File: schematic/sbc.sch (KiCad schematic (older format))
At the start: 17 parts

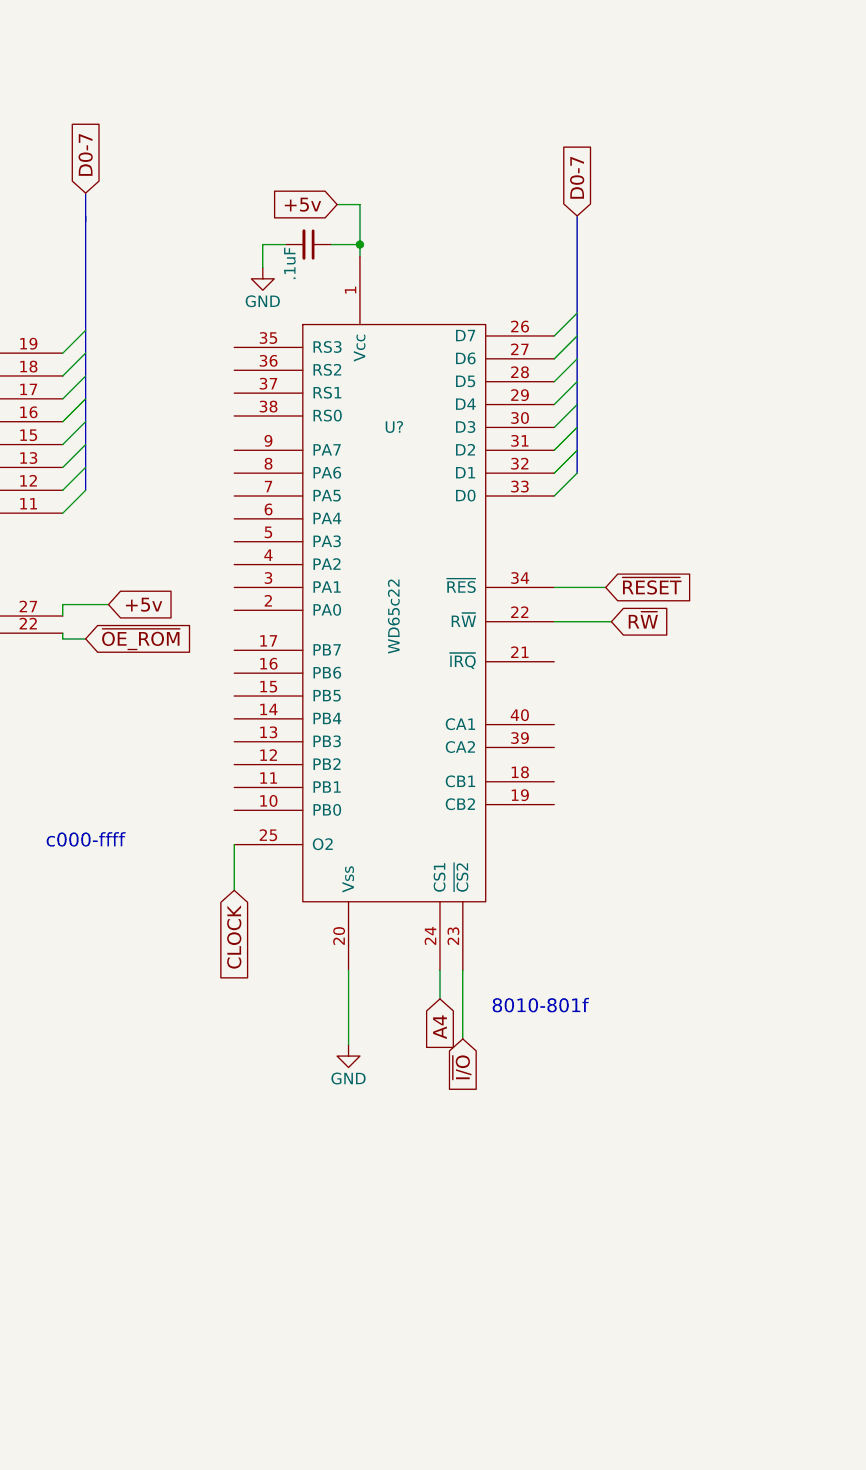
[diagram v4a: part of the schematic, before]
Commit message: Added LEDs to sbc schematic
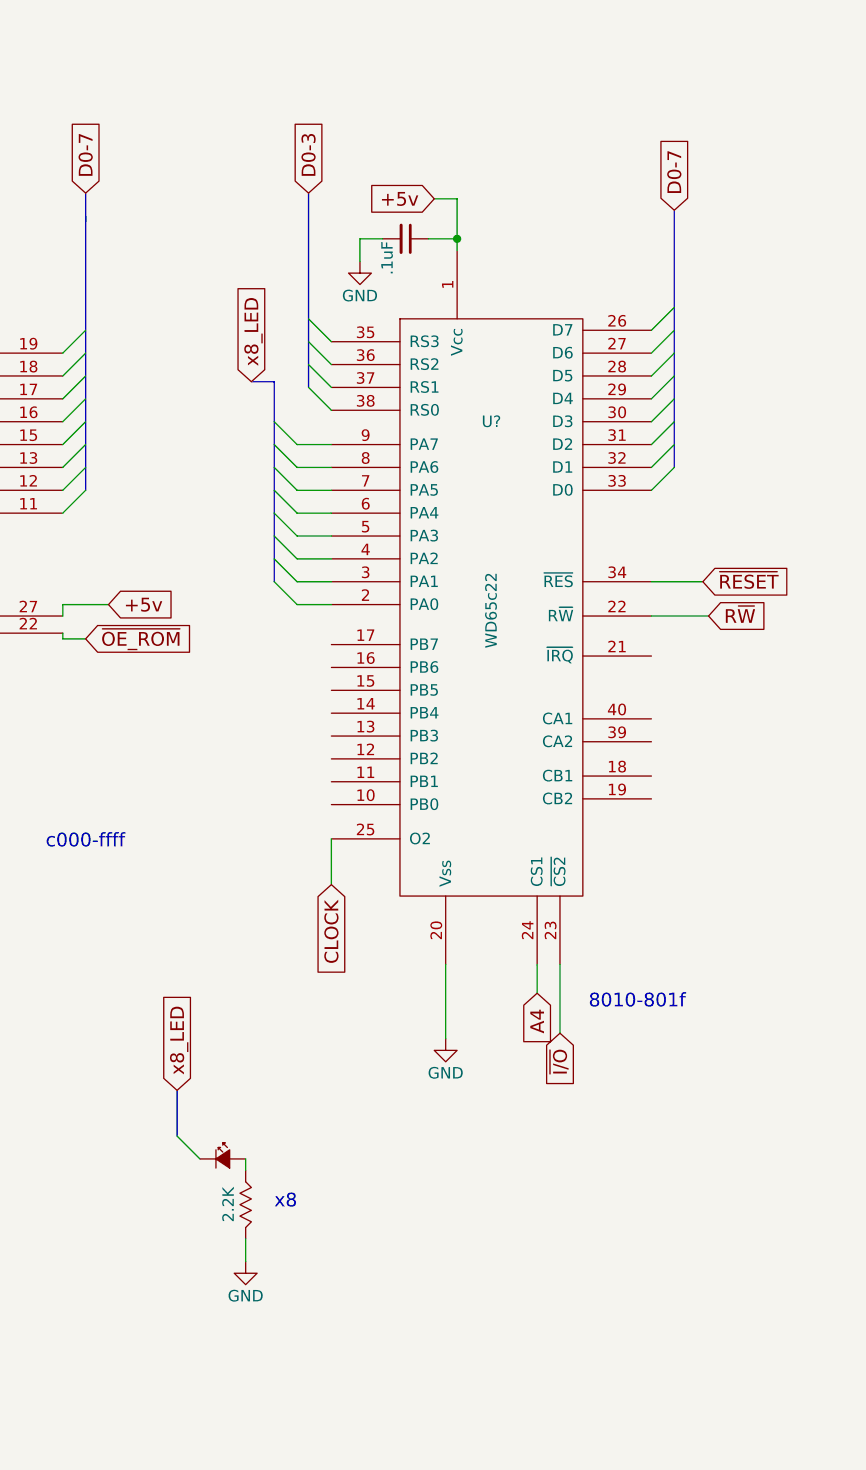
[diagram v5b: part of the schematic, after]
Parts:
- added D?: Led_Small, symbol Led_Small
- added R?: 2.2K, symbol Rsqig
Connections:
- net GND: now also R?.2
- new net: D?.2 (A), R?.1
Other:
- note added: "x8"
- moved on the sheet: U?
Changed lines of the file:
@@
 L WD65c22 U?
 U 1 1 58164F61
-P 9300 2900
-F 0 "U?" H 9300 3300 50  0000 C CNN
-F 1 "WD65c22" V 9300 2475 50  0000 C CNN
-F 2 "" H 9300 2900 50  0000 C CNN
-F 3 "" H 9300 2900 50  0000 C CNN
-	1    9300 2900
+P 9725 2875
+F 0 "U?" H 9725 3275 50  0000 C CNN
+F 1 "WD65c22" V 9725 2450 50  0000 C CNN
+F 2 "" H 9725 2875 50  0000 C CNN
+F 3 "" H 9725 2875 50  0000 C CNN
+	1    9725 2875
 	1    0    0    -1
 $EndComp
@@
 	7850 2175 7950 2075
 Entry Wire Line
-	10000 2800 10100 2700
-Entry Wire Line
-	10000 2700 10100 2600
-Entry Wire Line
-	10000 2600 10100 2500
-Entry Wire Line
-	10000 2500 10100 2400
-Entry Wire Line
-	10000 2400 10100 2300
-Entry Wire Line
-	10000 2300 10100 2200
-Entry Wire Line
-	10000 2200 10100 2100
-Entry Wire Line
-	10000 2100 10100 2000
+	10425 2775 10525 2675
+Entry Wire Line
+	10425 2675 10525 2575
+Entry Wire Line
+	10425 2575 10525 2475
+Entry Wire Line
+	10425 2475 10525 2375
+Entry Wire Line
+	10425 2375 10525 2275
+Entry Wire Line
+	10425 2275 10525 2175
+Entry Wire Line
+	10425 2175 10525 2075
+Entry Wire Line
+	10425 2075 10525 1975
 Text GLabel 3650 3700 2    60   Input ~ 0
 ~IRQ~
@@
 D0-7
 Wire Bus Line
-	10100 1575 10100 2700
+	10525 1550 10525 2675
 Wire Bus Line
 	7950 1575 7950 2775
@@
 Wire Bus Line
 	7950 1475 7950 1600
-Text GLabel 9500 5000 3    60   Input ~ 0
+Text GLabel 9925 4975 3    60   Input ~ 0
 A4
 Wire Wire Line
-	9500 5000 9500 4875
-Text GLabel 9600 5175 3    60   Input ~ 0
+	9925 4975 9925 4850
+Text GLabel 10025 5150 3    60   Input ~ 0
 ~I/O~
 Wire Wire Line
-	9600 5175 9600 4875
+	10025 5150 10025 4850
 Text GLabel 4900 6550 2    60   Input ~ 0
 ~I/O~
@@
 Wire Wire Line
 	4075 6350 4900 6350
-Text Notes 9725 5075 0    60   ~ 0
+Text Notes 10150 5050 0    60   ~ 0
 8010-801f
 Text Notes 7775 4350 0    60   ~ 0
@@
 L GND #PWR?
 U 1 1 58336CFD
-P 9100 5200
-F 0 "#PWR?" H 9100 4950 50  0001 C CNN
-F 1 "GND" H 9100 5050 50  0000 C CNN
-F 2 "" H 9100 5200 50  0000 C CNN
-F 3 "" H 9100 5200 50  0000 C CNN
-	1    9100 5200
-	1    0    0    -1
-$EndComp
-Wire Wire Line
-	9100 4875 9100 5200
-Text GLabel 9050 1525 0    60   Input ~ 0
+P 9525 5175
+F 0 "#PWR?" H 9525 4925 50  0001 C CNN
+F 1 "GND" H 9525 5025 50  0000 C CNN
+F 2 "" H 9525 5175 50  0000 C CNN
+F 3 "" H 9525 5175 50  0000 C CNN
+	1    9525 5175
+	1    0    0    -1
+$EndComp
+Wire Wire Line
+	9525 4850 9525 5175
+Text GLabel 9475 1500 0    60   Input ~ 0
 +5v
 $Comp
 L GND #PWR?
 U 1 1 58336E6C
-P 8725 1800
-F 0 "#PWR?" H 8725 1550 50  0001 C CNN
-F 1 "GND" H 8725 1650 50  0000 C CNN
-F 2 "" H 8725 1800 50  0000 C CNN
-F 3 "" H 8725 1800 50  0000 C CNN
-	1    8725 1800
+P 9150 1775
+F 0 "#PWR?" H 9150 1525 50  0001 C CNN
+F 1 "GND" H 9150 1625 50  0000 C CNN
+F 2 "" H 9150 1775 50  0000 C CNN
+F 3 "" H 9150 1775 50  0000 C CNN
+	1    9150 1775
 	1    0    0    -1
 $EndComp
@@
 L C_Small C?
 U 1 1 58336E9A
-P 8925 1700
-F 0 "C?" H 8935 1770 50  0001 L CNN
-F 1 ".1uF" H 8935 1620 50  0000 L CNN
-F 2 "" H 8925 1700 50  0000 C CNN
-F 3 "" H 8925 1700 50  0000 C CNN
-	1    8925 1700
+P 9350 1675
+F 0 "C?" H 9360 1745 50  0001 L CNN
+F 1 ".1uF" H 9360 1595 50  0000 L CNN
+F 2 "" H 9350 1675 50  0000 C CNN
+F 3 "" H 9350 1675 50  0000 C CNN
+	1    9350 1675
 	0    1    1    0
 $EndComp
 Wire Wire Line
-	9025 1700 9150 1700
-Wire Wire Line
-	9150 1525 9150 1750
-Wire Wire Line
-	9150 1525 9050 1525
-Connection ~ 9150 1700
-Wire Wire Line
-	8725 1800 8725 1700
-Wire Wire Line
-	8725 1700 8825 1700
-Text GLabel 10100 1575 1    60   Input ~ 0
+	9450 1675 9575 1675
+Wire Wire Line
+	9575 1500 9575 1725
+Wire Wire Line
+	9575 1500 9475 1500
+Connection ~ 9575 1675
+Wire Wire Line
+	9150 1775 9150 1675
+Wire Wire Line
+	9150 1675 9250 1675
+Text GLabel 10525 1550 1    60   Input ~ 0
 D0-7
-Text GLabel 10250 3350 2    60   Input ~ 0
+Text GLabel 10675 3325 2    60   Input ~ 0
 R~W~
-Text GLabel 10225 3200 2    60   Input ~ 0
+Text GLabel 10650 3175 2    60   Input ~ 0
 ~RESET~
-Text GLabel 8600 4525 3    60   Input ~ 0
+Text GLabel 9025 4500 3    60   Input ~ 0
 CLOCK
 Wire Wire Line
-	10000 3200 10225 3200
-Wire Wire Line
-	10000 3350 10250 3350
-Wire Wire Line
-	8600 4525 8600 4325
+	10425 3175 10650 3175
+Wire Wire Line
+	10425 3325 10675 3325
+Wire Wire Line
+	9025 4500 9025 4300
+Entry Wire Line
+	8925 2025 9025 2125
+Entry Wire Line
+	8925 2125 9025 2225
+Entry Wire Line
+	8925 2225 9025 2325
+Entry Wire Line
+	8925 2325 9025 2425
+Wire Bus Line
+	8925 2325 8925 1475
+Text GLabel 8925 1475 1    60   Input ~ 0
+D0-3
+Entry Wire Line
+	8775 2475 8875 2575
+Entry Wire Line
+	8775 2575 8875 2675
+Entry Wire Line
+	8775 2675 8875 2775
+Entry Wire Line
+	8775 2775 8875 2875
+Entry Wire Line
+	8775 2875 8875 2975
+Entry Wire Line
+	8775 2975 8875 3075
+Entry Wire Line
+	8775 3075 8875 3175
+Entry Wire Line
+	8775 3175 8875 3275
+Wire Wire Line
+	8875 2575 9025 2575
+Wire Wire Line
+	8875 2675 9025 2675
+Wire Wire Line
+	8875 2775 9025 2775
+Wire Wire Line
+	8875 2875 9025 2875
+Wire Wire Line
+	8875 2975 9025 2975
+Wire Wire Line
+	8875 3075 9025 3075
+Wire Wire Line
+	8875 3175 9025 3175
+Wire Wire Line
+	8875 3275 9025 3275
+Wire Bus Line
+	8775 3175 8775 2300
+Wire Bus Line
+	8775 2300 8675 2300
+Text GLabel 8675 2300 1    60   Input ~ 0
+x8_LED
+$Comp
+L Led_Small D?
+U 1 1 5833C3BD
+P 8550 5700
+F 0 "D?" H 8500 5825 50  0001 L CNN
+F 1 "Led_Small" H 8375 5600 50  0001 L CNN
+F 2 "" V 8550 5700 50  0000 C CNN
+F 3 "" V 8550 5700 50  0000 C CNN
+	1    8550 5700
+	1    0    0    -1
+$EndComp
+$Comp
+L GND #PWR?
+U 1 1 5833C420
+P 8650 6150
+F 0 "#PWR?" H 8650 5900 50  0001 C CNN
+F 1 "GND" H 8650 6000 50  0000 C CNN
+F 2 "" H 8650 6150 50  0000 C CNN
+F 3 "" H 8650 6150 50  0000 C CNN
+	1    8650 6150
+	1    0    0    -1
+$EndComp
+$Comp
+L Rsqig R?
+U 1 1 5833C450
+P 8650 5900
+F 0 "R?" V 8730 5900 50  0001 C CNN
+F 1 "2.2K" V 8575 5900 50  0000 C CNN
+F 2 "" V 8580 5900 50  0000 C CNN
+F 3 "" H 8650 5900 50  0000 C CNN
+	1    8650 5900
+	1    0    0    -1
+$EndComp
+Wire Wire Line
+	8650 6150 8650 6050
+Wire Wire Line
+	8650 5750 8650 5700
+Entry Wire Line
+	8350 5600 8450 5700
+Wire Bus Line
+	8350 5600 8350 5400
+Text GLabel 8350 5400 1    60   Input ~ 0
+x8_LED
+Text Notes 8775 5925 0    60   ~ 0
+x8
 $EndSCHEMATC

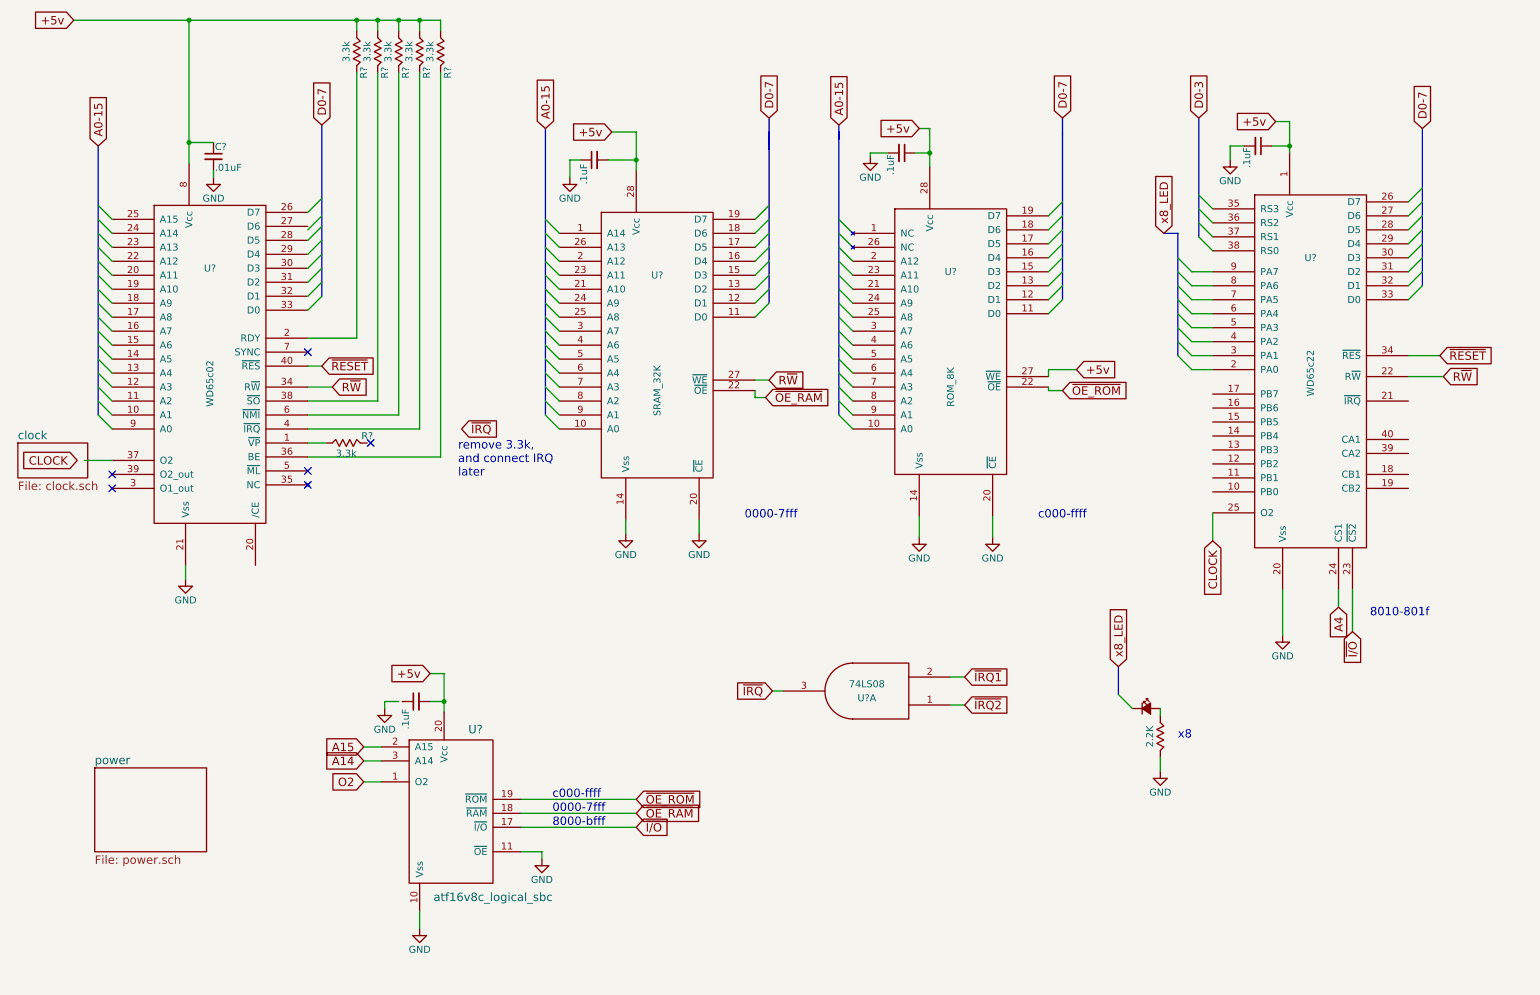
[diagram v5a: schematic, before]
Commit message: sbc added FRAM to schematic
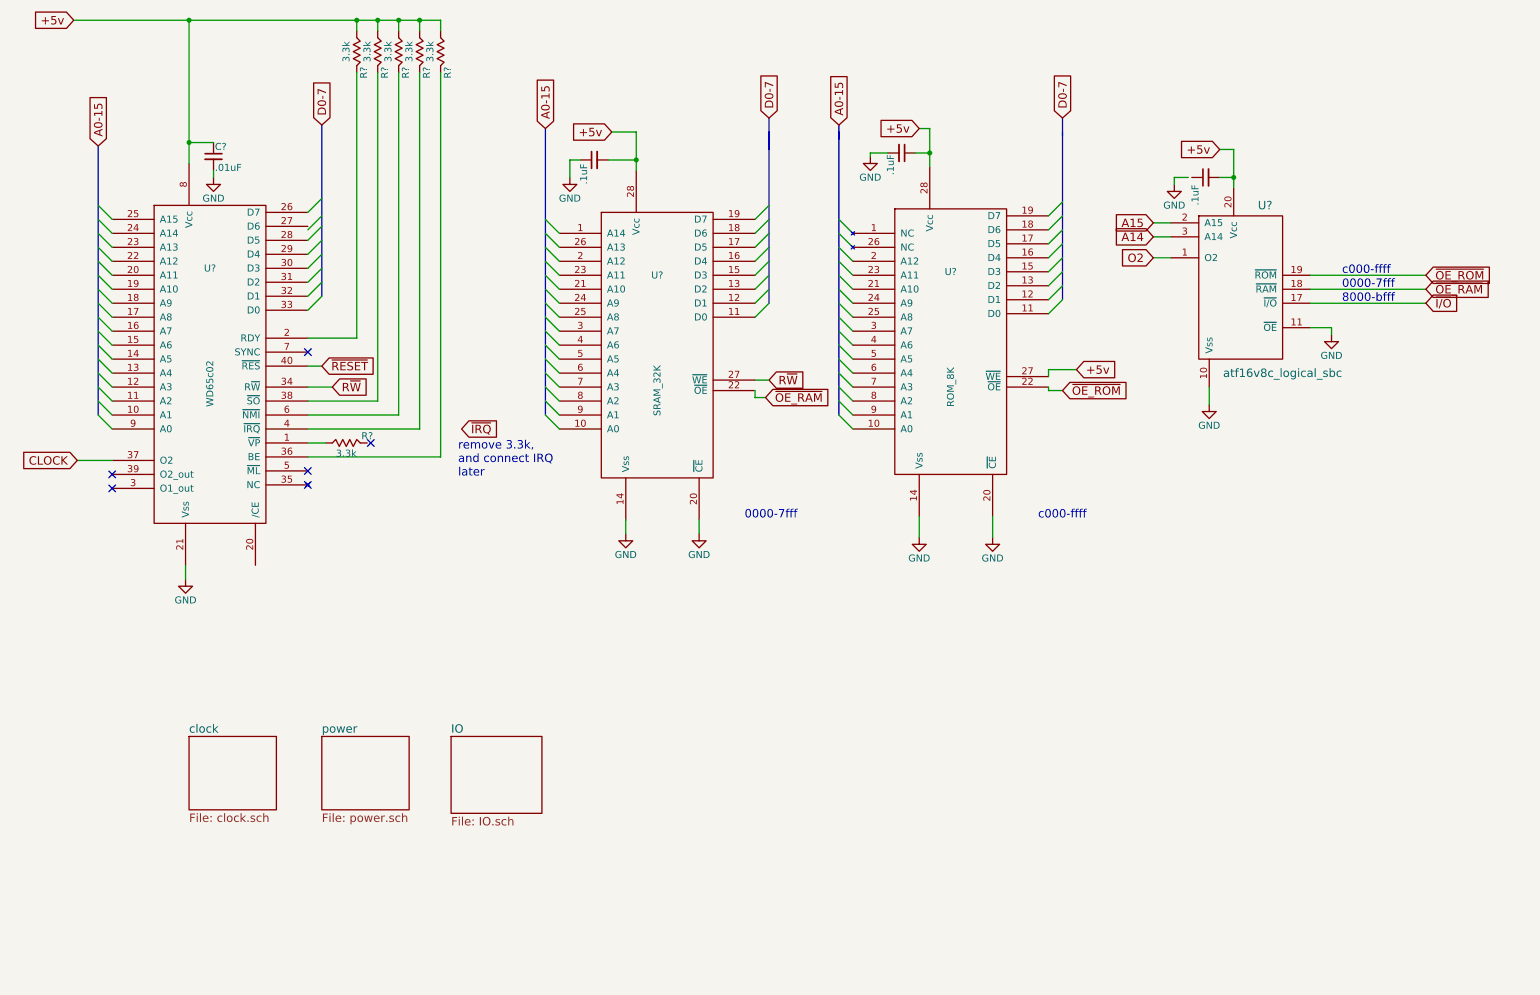
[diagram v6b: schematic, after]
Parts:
- removed C?: .1uF, symbol C_Small
- removed D?: Led_Small, symbol Led_Small
- removed R?: 2.2K, symbol Rsqig
- removed U?: WD65c22, symbol WD65c22
- removed U?: 74LS08, symbol 74LS08
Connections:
- net CLOCK: now also U?.37 (O2)
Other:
- note removed: "8010-801f"
- note removed: "x8"
- moved on the sheet: U?

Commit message: SBC Schematic final
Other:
- note added: "December 10th, 2016"
- note added: "Micheal Burin - ECEN 5613"
- note added: "Single Board Computer - Main"
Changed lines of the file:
@@
 F1 "IO.sch" 60
 $EndSheet
+Text Notes 7000 6675 0    60   ~ 0
+Micheal Burin - ECEN 5613
+Text Notes 7350 7500 0    60   ~ 0
+Single Board Computer - Main
+Text Notes 8150 7650 0    60   ~ 0
+December 10th, 2016
 $EndSCHEMATC
